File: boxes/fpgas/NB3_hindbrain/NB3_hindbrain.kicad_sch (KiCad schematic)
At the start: 18 parts, among them IC1 NOR_Flash_W25Q32JVSSIQ, IC2 FPGA_ICE40UP5K-SG48I, J1 MicroUSB_10103594-0001LF, U1 USBtoSPI_FT4232HL, U2 EEPROM_93LC56BT-I-OT, Y1 Osc_12MHz_ECS-2520MV-120-BN-TR

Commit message: Tweaks to NB3_hindbrain
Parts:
- added C1, C2, C8, C9: 10uF, Capacitor_SMD:C_0603_1608Metric, symbol Device:C
- added C10, C3, C4, C5, C6: 100nF, Capacitor_SMD:C_0402_1005Metric, symbol Device:C
- added J2, J3: Conn_01x20_Male, Connector_PinHeader_2.54mm:PinHeader_1x20_P2.54mm_Vertical, symbol Connector:Conn_01x20_Male
- C11: renamed from C?; footprint (none) -> Capacitor_SMD:C_0402_1005Metric
- C7: renamed from C1; value 100nF -> 3.3uF; footprint (none) -> Capacitor_SMD:C_0603_1608Metric
- R1, R2, R3, R4, R5, R6, R7, R8: footprint (none) -> Resistor_SMD:R_0402_1005Metric
- renumbered IC2 to IC1, IC1 to IC2, VR2 to VR1, VR1 to VR2
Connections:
- net +3V3: now also IC2.8 (VCC), U1.20 (VCCIO), U1.31 (VCCIO), U1.42 (VCCIO), U1.50 (VREGIN), U1.56 (VCCIO), VR1.2 (VOUT_2), VR1.4 (VOUT_4), C10.2, C6.1, C9.1; no longer C7.2
- net GND: now also IC2.4 (GND), VR1.1 (GND), VR2.1 (GND), C1.2, C10.1, C2.2, C3.2, C4.2, C5.2, C6.2, C8.2, C9.2
- net +1V8: now reaches U1.12 (VCORE)
- net +1V8: now also C7.2, U1.37 (VCORE), U1.49 (VREGOUT), U1.64 (VCORE)
- net +5V: now reaches VR2.2 (VIN_1)
- net +5V: now also VR1.3 (VIN), VR2.4 (VIN_2), C1.1, C2.1, C3.1, C4.1
- net +1V2: now reaches VR2.3 (VOUT)
- net +1V2: now also C5.1, C8.1
- net FPGA_SO: now reaches IC1.14 (IOB_32A_SPI_SO)
- net FPGA_SO: now also IC2.5 (DI_(IO0))
- net FPGA_SCK: now reaches IC1.15 (IOB_34A_SPI_SCK)
- net FPGA_SCK: now also IC2.6 (CLK)
- net FPGA_SS: now reaches IC1.16 (IOB_35B_SPI_SS)
- net FPGA_SI: now reaches IC1.17 (IOB_33B_SPI_SI_1)
- net FPGA_SI: now also IC2.2 (DO_(IO1))
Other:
- note added: "Needs bypass (and beeds)"
- note added: "Voltage Regulators (LDO) +3.3V +1.2V"
- note removed: "Voltage Regulators (LDO) - +3.3V - +1.2V"
- moved on the sheet: C11, C7, IC1, IC2, U2, VR1, VR2, Y1

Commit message: Work on NB3_hindbrain
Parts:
- renumbered R6 to R4, R4 to R5, R5 to R6
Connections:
- net FPGA_SCK: now also U1.26 (BDBUS0); no longer IC2.6 (CLK)
- net FPGA_SI: now also U1.27 (BDBUS1); no longer IC2.2 (DO_(IO1))
- net FPGA_SO: now also U1.28 (BDBUS2); no longer IC2.5 (DI_(IO0))
- net FPGA_SS: now also U1.30 (BDBUS4)
- net FLASH_SCK: now reaches U1.16 (ADBUS0)
- net FLASH_SI: now reaches U1.17 (ADBUS1)
- net FLASH_SO: now reaches U1.18 (ADBUS2)
- net FLASH_SS: now reaches U1.21 (ADBUS4)
- net FLASH_SS: now also IC2.1 (/CS)
- net CDONE: now reaches U1.23 (ADBUS6)
- net CDONE: now also IC1.7 (CDONE), U1.33 (BDBUS6)
- net CRESET_B: now reaches U1.24 (ADBUS7)
- net CRESET_B: now also IC1.8 (CRESET_B), U1.34 (BDBUS7)
- no-connect marks 3 -> 23
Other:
- moved on the sheet: R1, R2, R3, R4

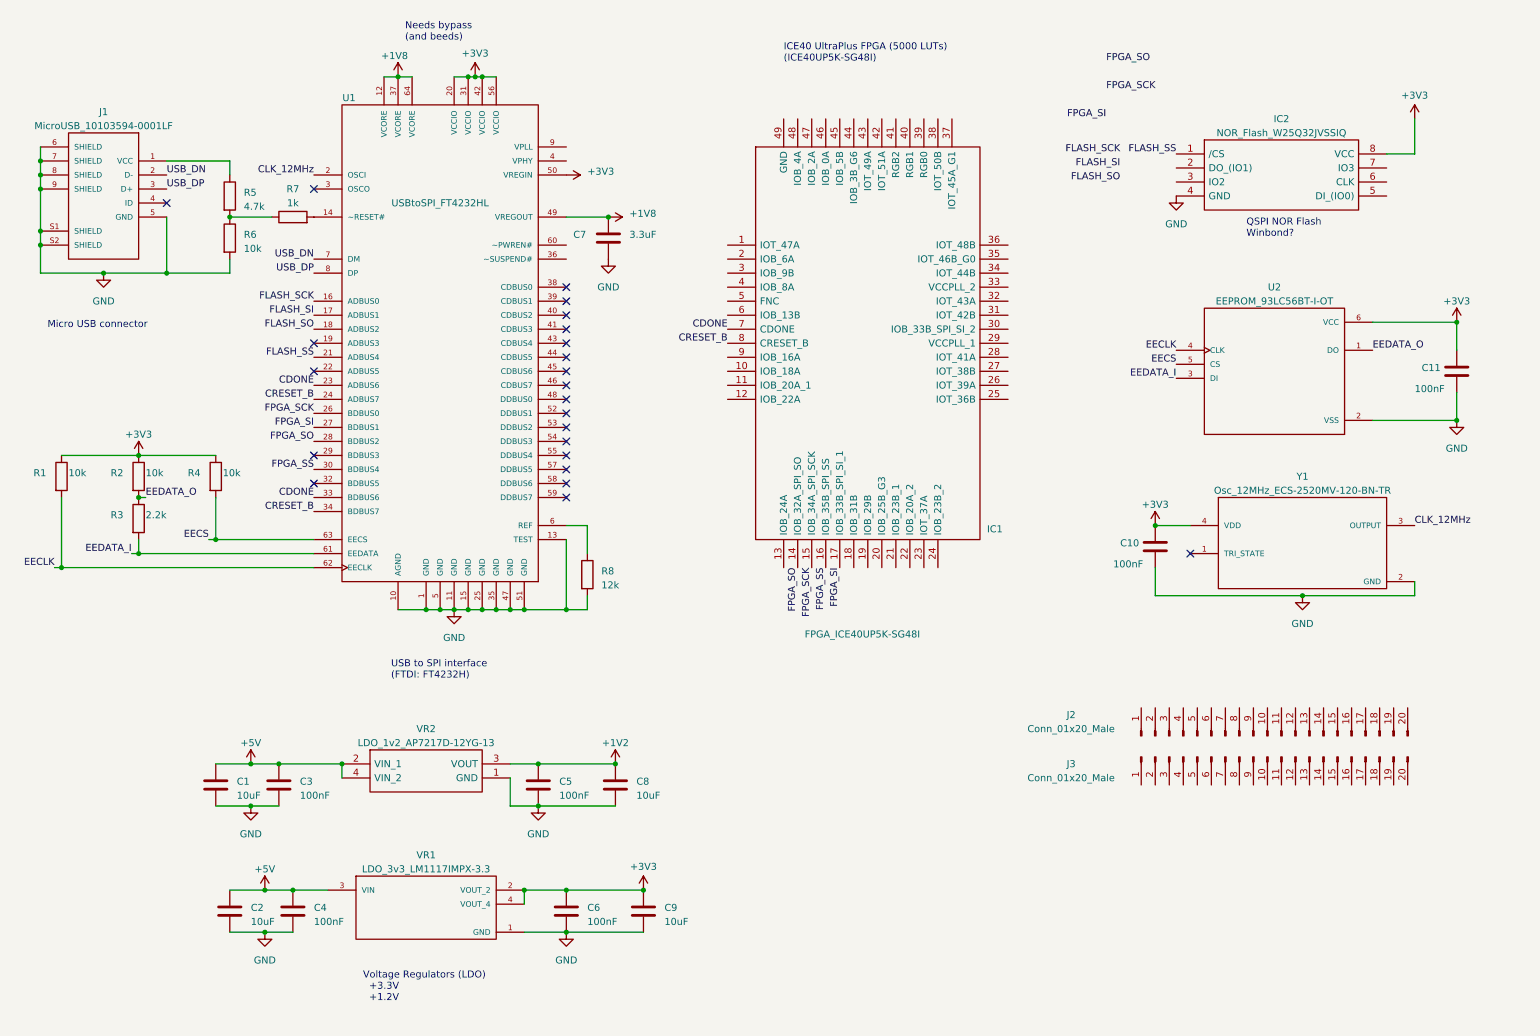
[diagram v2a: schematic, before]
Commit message: Update NB3_hindbrain (3D models)
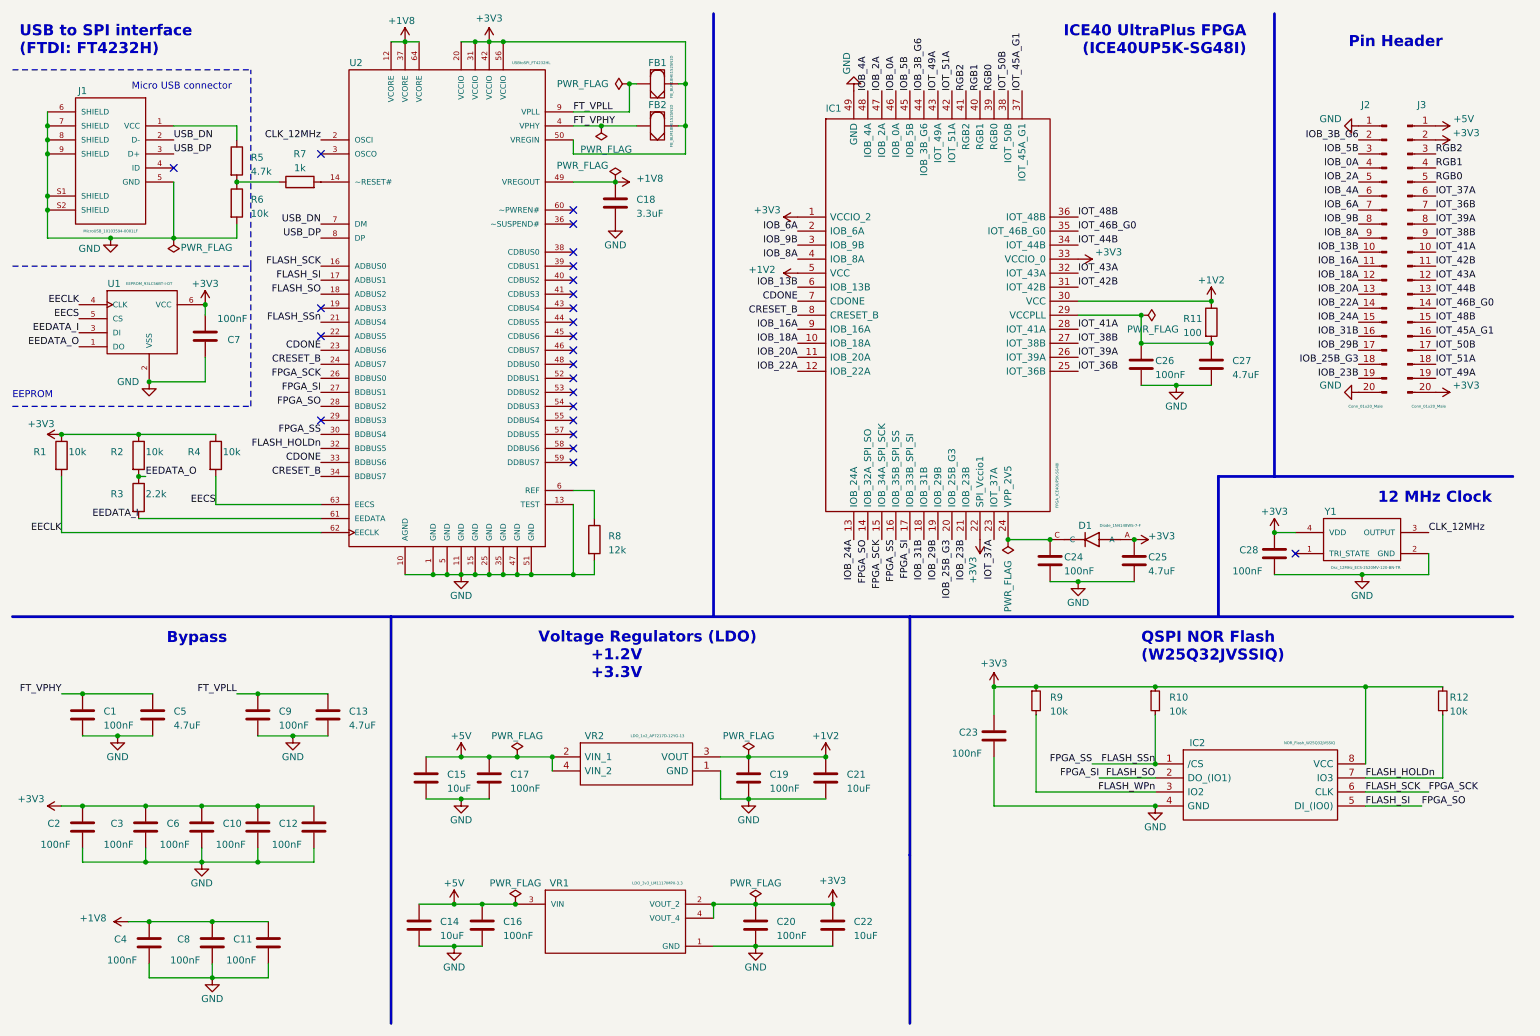
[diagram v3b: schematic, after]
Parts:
- added C1, C24, C26, C9: 100nF, symbol Device:C
- added C10, C11, C12, C2, C23, C3, C4, C6, C8: 100nF, Capacitor_SMD:C_0402_1005Metric, symbol Device:C
- added C13, C25, C27, C5: 4.7uF, symbol Device:C
- added D1: Diode_1N4148WS-7-F, NB3_hindbrain:Diode_1N4148WS-7-F, symbol NB3_hindbrain:Diode_1N4148WS-7-F
- added FB1, FB2: FB_BLM18HE152SN1D, NB3_hindbrain:FB_BLM18HE152SN1D, symbol NB3_hindbrain:FB_BLM18HE152SN1D
- added R10, R12, R9: 10k, symbol Device:R_Small
- added R11: 100, symbol Device:R
- renumbered C2 to C14, C1 to C15, C4 to C16, C3 to C17, C7 to C18, C5 to C19, C6 to C20, C8 to C21, C9 to C22, C10 to C28, C11 to C7, J3 to J2, J2 to J3, U2 to U1, U1 to U2
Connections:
- net FPGA_SCK is gone; now on net FLASH_SCK: IC1.15 (IOB_34A_SPI_SCK), U2.26 (BDBUS0)
- net FPGA_SI is gone; now on net FLASH_SO: IC1.17 (IOB_33B_SPI_SI), U2.27 (BDBUS1)
- net FPGA_SO is gone; now on net FLASH_SI: IC1.14 (IOB_32A_SPI_SO), U2.28 (BDBUS2)
- net FPGA_SS is gone; now on net FLASH_SSn: IC1.16 (IOB_35B_SPI_SS), U2.30 (BDBUS4)
- net +1V2: now also IC1.30 (VCC), IC1.5 (VCC), R11.1
- net +1V8: now also C11.2, C4.2, C8.2
- net +3V3: now also C7.1, IC1.1 (VCCIO_2), IC1.22 (SPI_Vccio1), IC1.33 (VCCIO_0), J3.2 (Pin_2), J3.20 (Pin_20), C10.2, C12.2, C2.2, C23.2, C25.1, C3.2, C6.2, D1.A, FB1.2, FB2.2, R10.1, R12.2, R9.1; no longer C7.2
- net +5V: now also J3.1 (Pin_1)
- net FLASH_SCK: now also IC2.6 (CLK)
- net FLASH_SI: now also IC2.5 (DI_(IO0))
- net FLASH_SO: now also IC2.2 (DO_(IO1))
- net GND: now also C7.2, IC1.49 (GND), J2.1 (Pin_1), J2.20 (Pin_20), C1.2, C10.1, C11.1, C12.1, C13.2, C2.1, C23.1, C24.2, C25.2, C26.2, C27.2, C3.1, C4.1, C5.2, C6.1, C8.1, C9.2; no longer C7.1
- net FLASH_HOLDn: now reaches U2.32 (BDBUS5)
- net FLASH_HOLDn: now also IC2.7 (IO3), R12.1
- net FT_VPHY: now reaches U2.4 (VPHY)
- net FT_VPHY: now also C1.1, C5.1, FB2.1
- net FT_VPLL: now reaches U2.9 (VPLL)
- net FT_VPLL: now also C13.1, C9.1, FB1.1
- net IOT_41A: now reaches J3.10 (Pin_10)
- net IOT_41A: now also IC1.28 (IOT_41A)
- net IOT_42B: now reaches J3.11 (Pin_11)
- net IOT_42B: now also IC1.31 (IOT_42B)
- net IOT_43A: now reaches J3.12 (Pin_12)
- net IOT_43A: now also IC1.32 (IOT_43A)
- net IOT_44B: now reaches J3.13 (Pin_13)
- net IOT_44B: now also IC1.34 (IOT_44B)
- net IOT_46B_G0: now reaches J3.14 (Pin_14)
- net IOT_46B_G0: now also IC1.35 (IOT_46B_G0)
- net IOT_48B: now reaches J3.15 (Pin_15)
- net IOT_48B: now also IC1.36 (IOT_48B)
- net IOT_45A_G1: now reaches J3.16 (Pin_16)
- net IOT_45A_G1: now also IC1.37 (IOT_45A_G1)
- net IOT_50B: now reaches J3.17 (Pin_17)
- net IOT_50B: now also IC1.38 (IOT_50B)
- net IOT_51A: now reaches J3.18 (Pin_18)
- net IOT_51A: now also IC1.42 (IOT_51A)
- net IOT_49A: now reaches J3.19 (Pin_19)
- net IOT_49A: now also IC1.43 (IOT_49A)
- net RGB2: now reaches J3.3 (Pin_3)
- net RGB2: now also IC1.41 (RGB2)
- net RGB1: now reaches J3.4 (Pin_4)
- net RGB1: now also IC1.40 (RGB1)
- net RGB0: now reaches J3.5 (Pin_5)
- net RGB0: now also IC1.39 (RGB0)
- net IOT_37A: now reaches J3.6 (Pin_6)
- net IOT_37A: now also IC1.23 (IOT_37A)
- net IOT_36B: now reaches J3.7 (Pin_7)
- net IOT_36B: now also IC1.25 (IOT_36B)
- net IOT_39A: now reaches J3.8 (Pin_8)
- net IOT_39A: now also IC1.26 (IOT_39A)
- net IOT_38B: now reaches J3.9 (Pin_9)
- net IOT_38B: now also IC1.27 (IOT_38B)
- net IOB_18A: now reaches IC1.10 (IOB_18A)
- net IOB_18A: now also J2.12 (Pin_12)
- net IOB_20A: now reaches IC1.11 (IOB_20A)
- net IOB_20A: now also J2.13 (Pin_13)
- net IOB_22A: now reaches IC1.12 (IOB_22A)
- net IOB_22A: now also J2.14 (Pin_14)
- net IOB_24A: now reaches IC1.13 (IOB_24A)
- net IOB_24A: now also J2.15 (Pin_15)
- net IOB_31B: now reaches IC1.18 (IOB_31B)
- net IOB_31B: now also J2.16 (Pin_16)
- net IOB_29B: now reaches IC1.19 (IOB_29B)
- net IOB_29B: now also J2.17 (Pin_17)
- net IOB_6A: now reaches IC1.2 (IOB_6A)
- net IOB_6A: now also J2.7 (Pin_7)
- net IOB_25B_G3: now reaches IC1.20 (IOB_25B_G3)
- net IOB_25B_G3: now also J2.18 (Pin_18)
- net IOB_23B: now reaches IC1.21 (IOB_23B)
- net IOB_23B: now also J2.19 (Pin_19)
- net at IC1.24 (VPP_2V5): now also C24.1, D1.C
- net at IC1.29 (VCCPLL): now also C26.1, C27.1, R11.2
- net IOB_9B: now reaches IC1.3 (IOB_9B)
- net IOB_9B: now also J2.8 (Pin_8)
- net IOB_8A: now reaches IC1.4 (IOB_8A)
- net IOB_8A: now also J2.9 (Pin_9)
- net IOB_3B_G6: now reaches IC1.44 (IOB_3B_G6)
- net IOB_3B_G6: now also J2.2 (Pin_2)
- net IOB_5B: now reaches IC1.45 (IOB_5B)
- net IOB_5B: now also J2.3 (Pin_3)
- net IOB_0A: now reaches IC1.46 (IOB_0A)
- net IOB_0A: now also J2.4 (Pin_4)
- net IOB_2A: now reaches IC1.47 (IOB_2A)
- net IOB_2A: now also J2.5 (Pin_5)
- net IOB_4A: now reaches IC1.48 (IOB_4A)
- net IOB_4A: now also J2.6 (Pin_6)
- net IOB_13B: now reaches IC1.6 (IOB_13B)
- net IOB_13B: now also J2.10 (Pin_10)
- net IOB_16A: now reaches IC1.9 (IOB_16A)
- net IOB_16A: now also J2.11 (Pin_11)
- net FLASH_WPn: now reaches IC2.3 (IO2)
- net FLASH_WPn: now also R9.2
- net FLASH_SS renamed FLASH_SSn
- net FLASH_SSn: now also R10.2
- no-connect marks 23 -> 24
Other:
- note added: "12 MHz Clock"
- note added: "Bypass"
- note added: "EEPROM"
- note added: "ICE40 UltraPlus FPGA (ICE40UP5K-SG48I)"
- note added: "Pin Header"
- note added: "QSPI NOR Flash (W25Q32JVSSIQ)"
- note added: "Voltage Regulators (LDO) +1.2V +3.3V"
- note removed: "ICE40 UltraPlus FPGA (5000 LUTs) (ICE40UP5K-SG48I)"
- note removed: "Needs bypass (and beeds)"
- note removed: "QSPI NOR Flash Winbond?"
- note removed: "Voltage Regulators (LDO) +3.3V +1.2V"
- moved on the sheet: C14, C15, C16, C17, C18, C19, C20, C21, C22, C28, C7, IC1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

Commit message: NB£_hindbrain layout update
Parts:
- C1, C24, C26, C9: footprint (none) -> Capacitor_SMD:C_0402_1005Metric
- C13, C25, C27, C5: footprint (none) -> Capacitor_SMD:C_0603_1608Metric
- R10, R11, R12, R9: footprint (none) -> Resistor_SMD:R_0402_1005Metric
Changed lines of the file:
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@@
       (effects (font (size 1.27 1.27)) (justify left))
     )
-    (property "Footprint" "" (id 2) (at 198.12 137.16 0)
+    (property "Footprint" "Resistor_SMD:R_0402_1005Metric" (id 2) (at 198.12 137.16 0)
       (effects (font (size 1.27 1.27)) hide)
     )
@@
       (effects (font (size 1.27 1.27)) (justify left))
     )
-    (property "Footprint" "" (id 2) (at 219.71 137.16 0)
+    (property "Footprint" "Resistor_SMD:R_0402_1005Metric" (id 2) (at 219.71 137.16 0)
       (effects (font (size 1.27 1.27)) hide)
     )
@@
       (effects (font (size 1.27 1.27)) (justify right))
     )
-    (property "Footprint" "" (id 2) (at 271.78 137.16 0)
+    (property "Footprint" "Resistor_SMD:R_0402_1005Metric" (id 2) (at 271.78 137.16 0)
       (effects (font (size 1.27 1.27)) hide)
     )
@@
       (effects (font (size 1.27 1.27)) (justify left))
     )
-    (property "Footprint" "" (id 2) (at 228.092 68.58 90)
+    (property "Footprint" "Resistor_SMD:R_0402_1005Metric" (id 2) (at 228.092 68.58 90)
       (effects (font (size 1.27 1.27)) hide)
     )
@@
       (effects (font (size 1.27 1.27)) (justify left))
     )
-    (property "Footprint" "" (id 2) (at 26.3652 143.51 0)
+    (property "Footprint" "Capacitor_SMD:C_0402_1005Metric" (id 2) (at 26.3652 143.51 0)
       (effects (font (size 1.27 1.27)) hide)
     )
@@
       (effects (font (size 1.27 1.27)) (justify left))
     )
-    (property "Footprint" "" (id 2) (at 39.0652 143.51 0)
+    (property "Footprint" "Capacitor_SMD:C_0603_1608Metric" (id 2) (at 39.0652 143.51 0)
       (effects (font (size 1.27 1.27)) hide)
     )
@@
       (effects (font (size 1.27 1.27)) (justify left))
     )
-    (property "Footprint" "" (id 2) (at 58.1152 143.51 0)
+    (property "Footprint" "Capacitor_SMD:C_0402_1005Metric" (id 2) (at 58.1152 143.51 0)
       (effects (font (size 1.27 1.27)) hide)
     )
@@
       (effects (font (size 1.27 1.27)) (justify left))
     )
-    (property "Footprint" "" (id 2) (at 70.8152 143.51 0)
+    (property "Footprint" "Capacitor_SMD:C_0603_1608Metric" (id 2) (at 70.8152 143.51 0)
       (effects (font (size 1.27 1.27)) hide)
     )
@@
       (effects (font (size 1.27 1.27)) (justify left))
     )
-    (property "Footprint" "" (id 2) (at 201.6252 115.57 0)
+    (property "Footprint" "Capacitor_SMD:C_0402_1005Metric" (id 2) (at 201.6252 115.57 0)
       (effects (font (size 1.27 1.27)) hide)
     )
@@
       (effects (font (size 1.27 1.27)) (justify left))
     )
-    (property "Footprint" "" (id 2) (at 216.8652 115.57 0)
+    (property "Footprint" "Capacitor_SMD:C_0603_1608Metric" (id 2) (at 216.8652 115.57 0)
       (effects (font (size 1.27 1.27)) hide)
     )
@@
       (effects (font (size 1.27 1.27)) (justify left))
     )
-    (property "Footprint" "" (id 2) (at 218.1352 80.01 0)
+    (property "Footprint" "Capacitor_SMD:C_0402_1005Metric" (id 2) (at 218.1352 80.01 0)
       (effects (font (size 1.27 1.27)) hide)
     )
@@
       (effects (font (size 1.27 1.27)) (justify left))
     )
-    (property "Footprint" "" (id 2) (at 230.8352 80.01 0)
+    (property "Footprint" "Capacitor_SMD:C_0603_1608Metric" (id 2) (at 230.8352 80.01 0)
       (effects (font (size 1.27 1.27)) hide)
     )
@@
     )
     (path "/d2d3dc7c-806e-431c-830b-56c629c97c48"
-      (reference "C1") (unit 1) (value "100nF") (footprint "")
+      (reference "C1") (unit 1) (value "100nF") (footprint "Capacitor_SMD:C_0402_1005Metric")
     )
     (path "/0e936169-42b7-497d-bef0-f9aa66fbcbc0"
@@
     )
     (path "/123477a6-2d5c-4409-8d5b-b9967510a409"
-      (reference "C5") (unit 1) (value "4.7uF") (footprint "")
+      (reference "C5") (unit 1) (value "4.7uF") (footprint "Capacitor_SMD:C_0603_1608Metric")
     )
     (path "/f4bb4d1e-a94a-45f8-a273-0cbacb94b651"
@@
     )
     (path "/7783b287-2c47-43a7-937d-91b0675507c2"
-      (reference "C9") (unit 1) (value "100nF") (footprint "")
+      (reference "C9") (unit 1) (value "100nF") (footprint "Capacitor_SMD:C_0402_1005Metric")
     )
     (path "/d2711ed4-29e4-489b-b8ab-68a90e49148c"
@@
     )
     (path "/ab051052-b152-4366-a37d-4005fe1e5e0a"
-      (reference "C13") (unit 1) (value "4.7uF") (footprint "")
+      (reference "C13") (unit 1) (value "4.7uF") (footprint "Capacitor_SMD:C_0603_1608Metric")
     )
     (path "/2ac20cc7-94f5-458d-8796-8da298331639"
@@
     )
     (path "/e4d6e6fe-85f1-4519-af65-e99e79e6e81f"
-      (reference "C24") (unit 1) (value "100nF") (footprint "")
+      (reference "C24") (unit 1) (value "100nF") (footprint "Capacitor_SMD:C_0402_1005Metric")
     )
     (path "/f35fe422-6cae-44c0-a56a-ce1f6661308b"
-      (reference "C25") (unit 1) (value "4.7uF") (footprint "")
+      (reference "C25") (unit 1) (value "4.7uF") (footprint "Capacitor_SMD:C_0603_1608Metric")
     )
     (path "/c912f35a-caf1-48b4-a4b2-e801c12bb173"
-      (reference "C26") (unit 1) (value "100nF") (footprint "")
+      (reference "C26") (unit 1) (value "100nF") (footprint "Capacitor_SMD:C_0402_1005Metric")
     )
     (path "/53910f54-f210-4e16-ad37-c84c82201058"
-      (reference "C27") (unit 1) (value "4.7uF") (footprint "")
+      (reference "C27") (unit 1) (value "4.7uF") (footprint "Capacitor_SMD:C_0603_1608Metric")
     )
     (path "/3a496b09-99b7-46cf-87e7-92c28106120b"
@@
     )
     (path "/3a57b1c8-1c51-480b-912e-ca4a639e696b"
-      (reference "R9") (unit 1) (value "10k") (footprint "")
+      (reference "R9") (unit 1) (value "10k") (footprint "Resistor_SMD:R_0402_1005Metric")
     )
     (path "/3206e405-7085-42ad-8811-48985e33e958"
-      (reference "R10") (unit 1) (value "10k") (footprint "")
+      (reference "R10") (unit 1) (value "10k") (footprint "Resistor_SMD:R_0402_1005Metric")
     )
     (path "/c4bfccd1-2e83-4b0d-b622-d8d46284fa12"
-      (reference "R11") (unit 1) (value "100") (footprint "")
+      (reference "R11") (unit 1) (value "100") (footprint "Resistor_SMD:R_0402_1005Metric")
     )
     (path "/72d2176b-4d51-4bbe-adbd-9de9c85d317e"
-      (reference "R12") (unit 1) (value "10k") (footprint "")
+      (reference "R12") (unit 1) (value "10k") (footprint "Resistor_SMD:R_0402_1005Metric")
     )
     (path "/e6d0bcfa-e5cc-4dd2-9b5e-28605d9578ae"
